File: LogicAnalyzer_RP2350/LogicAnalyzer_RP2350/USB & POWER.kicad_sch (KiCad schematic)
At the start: 21 parts, among them J1 USB_C_Receptacle_USB2.0_16P, U1 NCP1117ST33T3G, U2 TPS2552DRVR-1

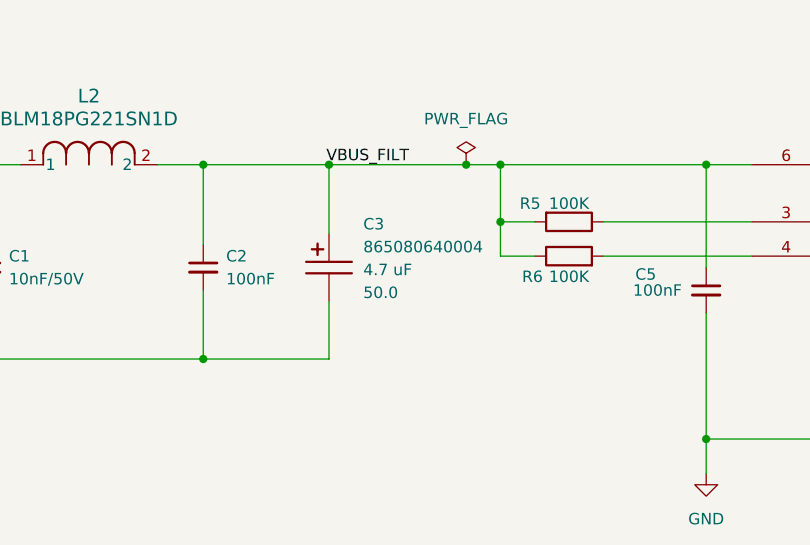
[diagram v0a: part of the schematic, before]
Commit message: Routing for Micro Controller Section Done
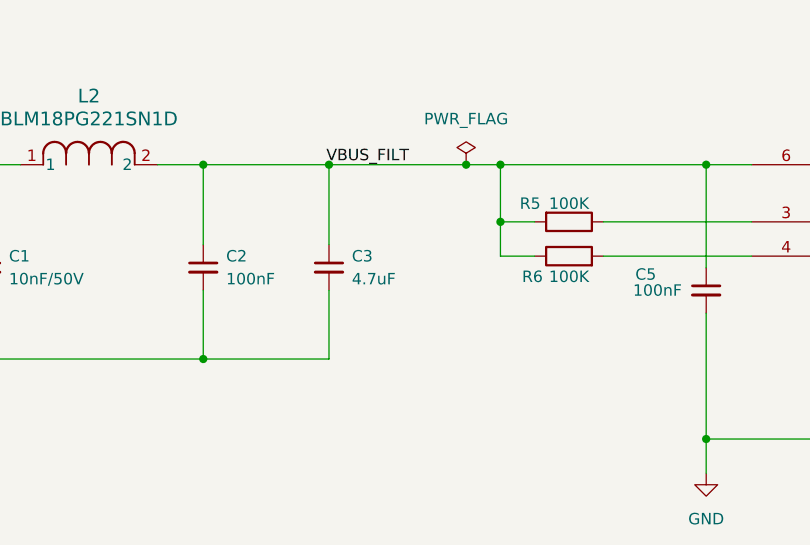
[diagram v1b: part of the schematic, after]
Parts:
- removed C3: 4.7 uF, Capacitor_SMD_Wurth:CP_Wurth_WCAP-ASLI-D4L5.5, symbol Capacitor_Wurth_WCAP-ASLI:D4L5.5_865080640004
- added C3: 4.7uF, Capacitor_SMD:C_0805_2012Metric_Pad1.18x1.45mm_HandSolder, symbol Device:C_Small
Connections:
- net GND: now also C3.2
- net VBUS_FILT: now also C3.1

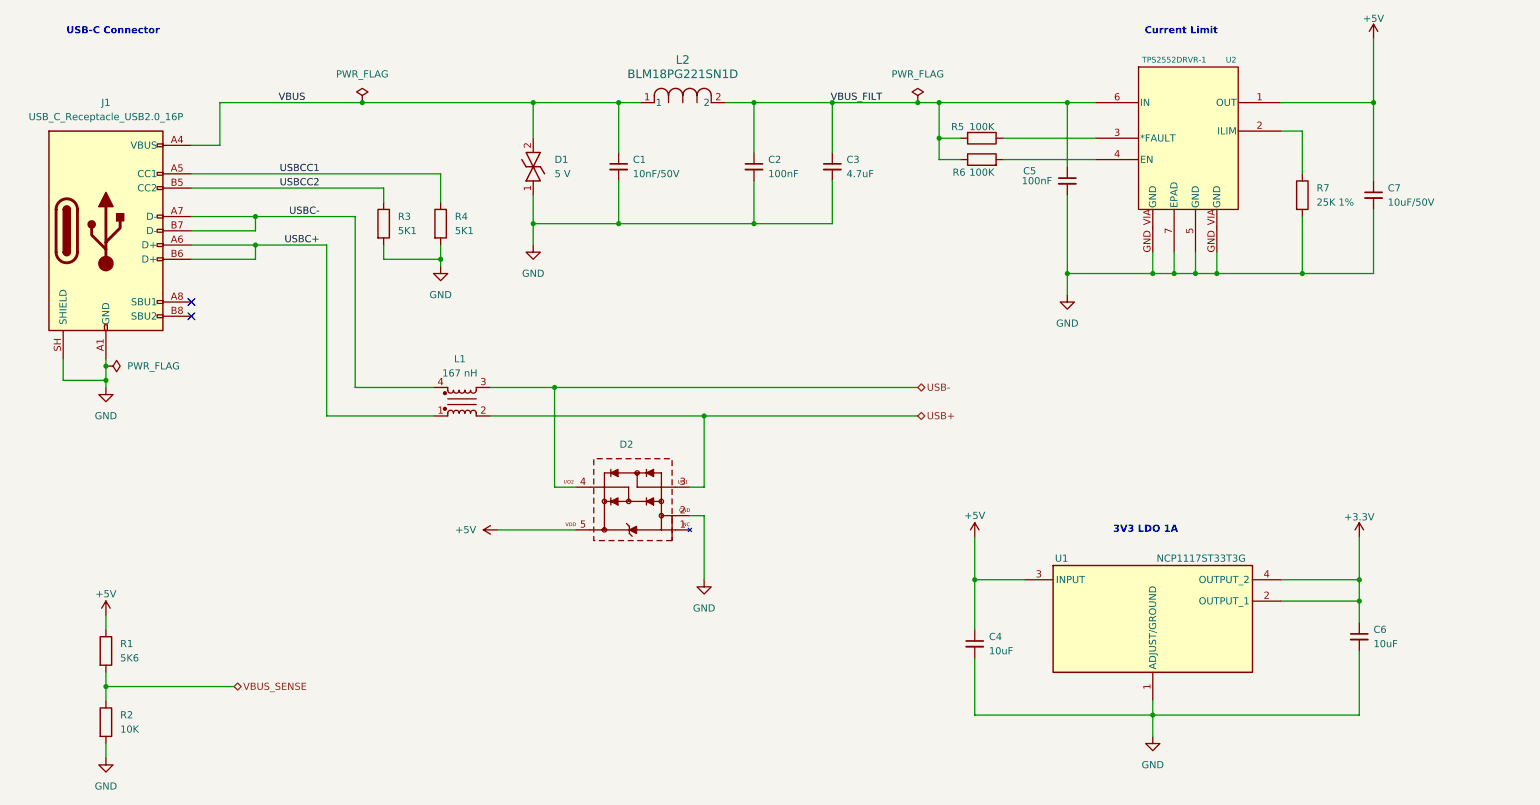
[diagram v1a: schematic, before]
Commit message: Initial Routing Done, almost there
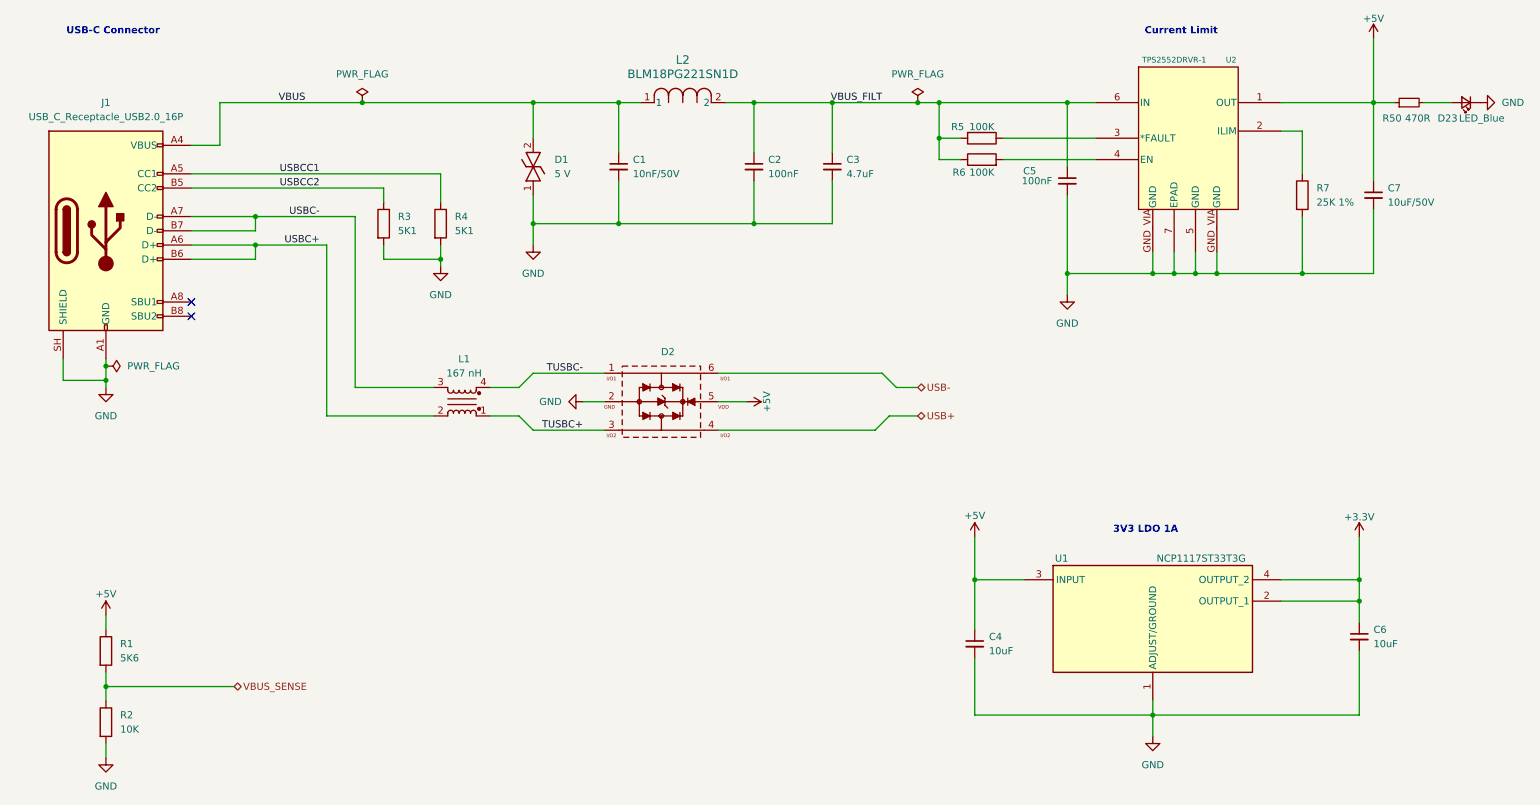
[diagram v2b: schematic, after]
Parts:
- removed D2: SOT23-5L_824011, Diode_SMD_Wurth:D_Wurth_WE-TVS-SOT23-5L, symbol Diode_Wurth_WE-TVS:SOT23-5L_824011
- added D2: SOT563_82400152, Diode_SMD_Wurth:D_Wurth_WE-TVS-SOT563, symbol Diode_Wurth_WE-TVS:SOT563_82400152
- added D23: LED_Blue, LED_SMD:LED_0603_1608Metric_Pad1.05x0.95mm_HandSolder, symbol Device:LED_Small
- added R50: 470R, Resistor_SMD:R_0603_1608Metric_Pad0.98x0.95mm_HandSolder, symbol Device:R_Small
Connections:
- net +5V: now also D2.5 (VDD), R50.1
- net GND: now also D2.2 (GND), D23.1 (K)
- net USB+: now also D2.4 (I/O4); no longer L1.2
- net USB-: now also D2.6 (I/O3); no longer L1.3
- net USBC+: now also L1.2; no longer L1.1
- net USBC-: now also L1.3; no longer L1.4
- new net: D23.2 (A), R50.2
- new net TUSBC+: D2.3 (I/O2), L1.1
- new net TUSBC-: D2.1 (I/O1), L1.4

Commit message: Correcting Diff pair USB
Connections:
- net TUSBC+: now also D2.4 (I/O4), L1.2; no longer D2.3 (I/O2), L1.1
- net TUSBC-: now also D2.6 (I/O3), L1.3; no longer D2.1 (I/O1), L1.4
- net USB+: now also L1.1; no longer D2.4 (I/O4)
- net USB-: now also L1.4; no longer D2.6 (I/O3)
- net USBC+: now also D2.3 (I/O2); no longer L1.2
- net USBC-: now also D2.1 (I/O1); no longer L1.3
